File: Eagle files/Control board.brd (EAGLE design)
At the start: 43.2 x 43.2 mm, 27 parts

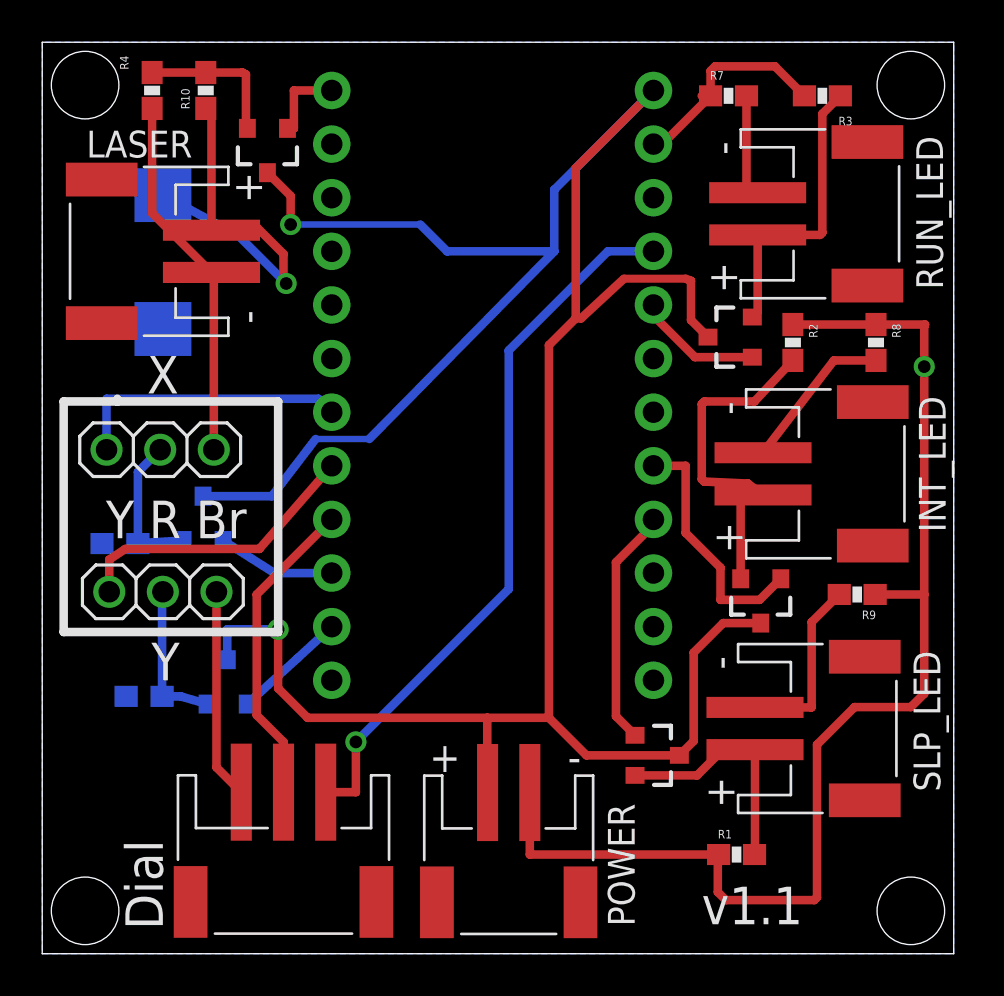
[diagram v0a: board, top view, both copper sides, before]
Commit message: added reverse diode protection on laser
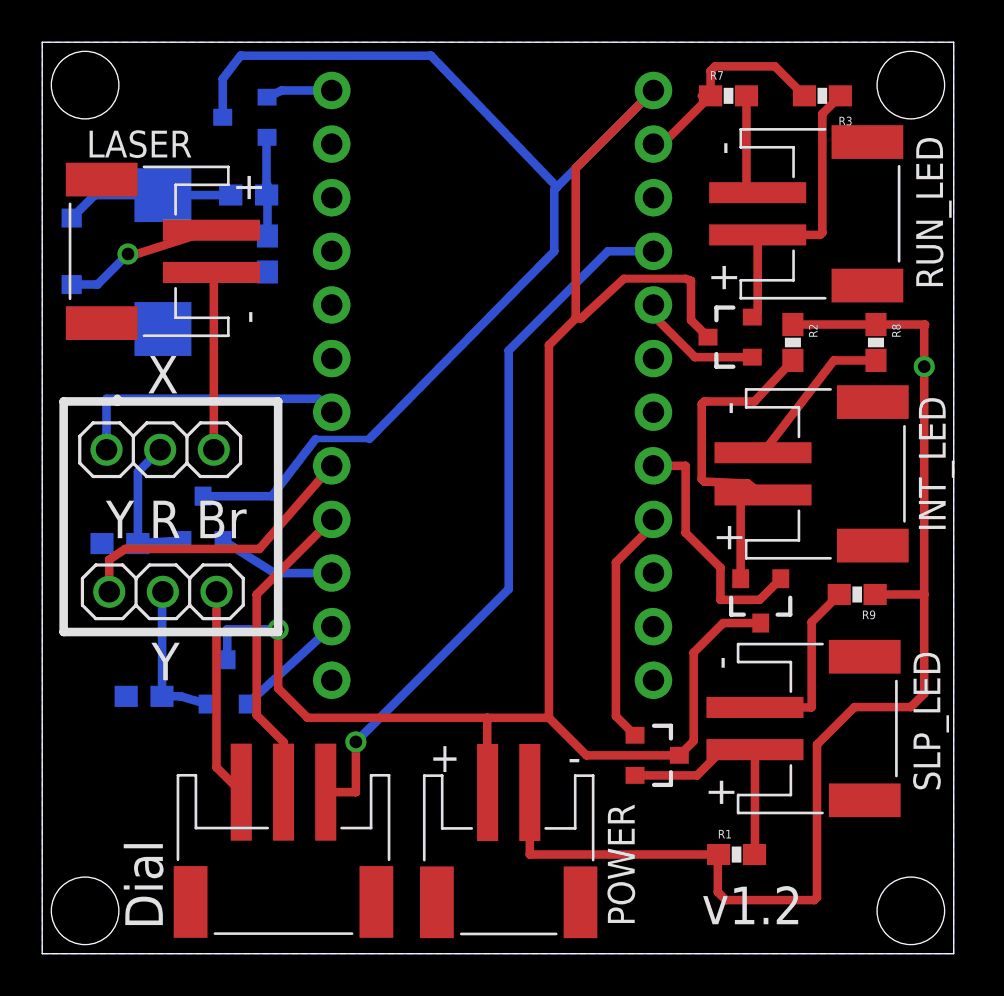
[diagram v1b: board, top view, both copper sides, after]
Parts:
- added D1: (no value), SparkFun-DiscreteSemi:SOD-123
- moved R4 9.48 mm to (10.7, 33.1), flipped to the bottom
- moved R10 5.35 mm to (9.78, 35.9), flipped to the bottom, turned to 180 degrees
- moved LASER_MOS 1.83 mm to (9.65, 39.6), flipped to the bottom, turned to 270 degrees
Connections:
- new net N$2: D1.C, LASER.1
- net N$1: now also D1.A; no longer LASER.1
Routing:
- net N$1: track 18.6 -> 7.98 mm, vias 1 -> 0
- net GND: track 96.0 -> 87.1 mm
- net N$2: track 0.00 -> 7.40 mm, vias 0 -> 1
- net VBAT: track 127.6 -> 132.5 mm, vias 2 -> 1
- net LASER_PWR: track 7.05 -> 5.21 mm
- net LASER_PIN: track 3.89 -> 3.13 mm
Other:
- board text added: "v1.2"
- board text removed: "v1.1"
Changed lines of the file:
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@@
 <wire x1="3.556" y1="26.162" x2="3.556" y2="26.289" width="0.4064" layer="25"/>
 <wire x1="43.18" y1="0" x2="43.18" y2="43.18" width="0" layer="20"/>
-<text x="31.242" y="1.397" size="1.778" layer="25">v1.1</text>
+<text x="31.242" y="1.397" size="1.778" layer="25">v1.2</text>
 </plain>
 <attributes>
@@
 <attribute name="NAME" x="37.719" y="39.243" size="0.4064" layer="25" font="vector"/>
 </element>
-<element name="LASER_MOS" library="SparkFun-DiscreteSemi" package="SOT23-3" value="200mA/50V" x="10.668" y="38.1" smashed="yes" rot="R180">
-<attribute name="PROD_ID" value="TRANS-00830" x="13.843" y="34.163" size="1.778" layer="27" rot="R180" display="off"/>
-</element>
-<element name="R4" library="SparkFun-Resistors" package="0603-RES" value="10K" x="5.207" y="40.894" smashed="yes" rot="R90">
-<attribute name="PROD_ID" value="RES-00824" x="1.27" y="37.719" size="1.778" layer="27" rot="R90" display="off"/>
-<attribute name="NAME" x="3.683" y="42.545" size="0.4064" layer="25" font="vector" rot="R270"/>
+<element name="LASER_MOS" library="SparkFun-DiscreteSemi" package="SOT23-3" value="200mA/50V" x="9.652" y="39.624" smashed="yes" rot="MR270">
+<attribute name="PROD_ID" value="TRANS-00830" x="5.715" y="42.799" size="1.778" layer="28" rot="MR270" display="off"/>
+</element>
+<element name="R4" library="SparkFun-Resistors" package="0603-RES" value="10K" x="10.668" y="33.147" smashed="yes" rot="MR90">
+<attribute name="PROD_ID" value="RES-00824" x="14.605" y="29.972" size="1.778" layer="28" rot="MR90" display="off"/>
+<attribute name="NAME" x="12.192" y="34.798" size="0.4064" layer="26" font="vector" rot="MR270"/>
 </element>
 <element name="X_MOS" library="SparkFun-DiscreteSemi" package="SOT23-3" value="2.6A/20V" x="7.62" y="20.574" smashed="yes" rot="MR0">
@@
 <attribute name="NAME" x="39.497" y="16.256" size="0.4064" layer="25" font="vector" rot="R180"/>
 </element>
-<element name="R10" library="SparkFun-Resistors" package="0603-RES" value="39" x="7.747" y="40.894" rot="R90">
-<attribute name="PROD_ID" value="RES-00824" x="7.747" y="40.894" size="1.778" layer="27" rot="R90" display="off"/>
+<element name="R10" library="SparkFun-Resistors" package="0603-RES" value="39" x="9.779" y="35.941" rot="MR180">
+<attribute name="PROD_ID" value="RES-00824" x="9.779" y="35.941" size="1.778" layer="28" rot="MR180" display="off"/>
 </element>
 <element name="C1" library="SparkFun-Capacitors" package="EIA7343" value="100uF" x="5.715" y="32.766" rot="MR90">
 <attribute name="PROD_ID" value="CAP-07890" x="5.715" y="32.766" size="1.778" layer="28" rot="MR90" display="off"/>
 </element>
+<element name="D1" library="SparkFun-DiscreteSemi" package="SOD-123" value="" x="1.397" y="33.274" rot="MR90"/>
 </elements>
 <signals>
@@
 <wire x1="41.148" y1="11.684" x2="41.783" y2="12.319" width="0.4064" layer="1"/>
 <wire x1="41.783" y1="12.319" x2="41.783" y2="17.018" width="0.4064" layer="1"/>
-<wire x1="8.128" y1="23.876" x2="8.128" y2="32.164" width="0.4064" layer="1"/>
 <wire x1="9.43" y1="7.653" x2="8.255" y2="8.828" width="0.4064" layer="1"/>
 <wire x1="8.255" y1="8.828" x2="8.255" y2="17.145" width="0.4064" layer="1"/>
@@
 <wire x1="8.128" y1="32.164" x2="7.747" y2="32.164" width="0.4064" layer="1"/>
 <wire x1="7.747" y1="32.274" x2="7.747" y2="32.164" width="0.4064" layer="1"/>
-<wire x1="8.018" y1="32.274" x2="5.207" y2="35.085" width="0.4064" layer="1"/>
-<wire x1="5.207" y1="35.085" x2="5.207" y2="40.044" width="0.4064" layer="1"/>
 <contactref element="JP1" pad="2"/>
 <wire x1="28.956" y1="38.354" x2="29.376" y2="38.354" width="0.4064" layer="1"/>
 <wire x1="29.376" y1="38.354" x2="31.662" y2="40.64" width="0.4064" layer="1"/>
+<wire x1="8.128" y1="32.164" x2="8.128" y2="23.876" width="0.4064" layer="1"/>
 <wire x1="8.128" y1="32.164" x2="8.018" y2="32.274" width="0" layer="19" extent="1-1"/>
 </signal>
@@
 <contactref element="JP4" pad="1"/>
 <contactref element="LASER_MOS" pad="1"/>
-<wire x1="11.618" y1="39.1" x2="11.922" y2="39.1" width="0.4064" layer="1"/>
-<wire x1="11.922" y1="39.1" x2="11.922" y2="40.894" width="0.4064" layer="1"/>
-<wire x1="11.922" y1="40.894" x2="13.716" y2="40.894" width="0.4064" layer="1"/>
+<wire x1="10.652" y1="40.574" x2="11.348" y2="40.894" width="0.4064" layer="16"/>
+<wire x1="11.348" y1="40.894" x2="13.716" y2="40.894" width="0.4064" layer="16"/>
 </signal>
 <signal name="AREF">
@@
 <contactref element="R4" pad="2"/>
 <contactref element="R10" pad="2"/>
-<wire x1="9.718" y1="39.1" x2="9.652" y2="39.166" width="0.4064" layer="1"/>
-<wire x1="9.652" y1="39.166" x2="9.652" y2="41.656" width="0.4064" layer="1"/>
-<wire x1="9.652" y1="41.656" x2="9.486" y2="41.744" width="0.4064" layer="1"/>
-<wire x1="9.486" y1="41.744" x2="7.747" y2="41.744" width="0.4064" layer="1"/>
-<wire x1="7.747" y1="41.744" x2="5.207" y2="41.744" width="0.4064" layer="1"/>
+<wire x1="10.629" y1="35.941" x2="10.629" y2="36.449" width="0.4064" layer="16"/>
+<wire x1="10.629" y1="36.449" x2="10.629" y2="38.651" width="0.4064" layer="16"/>
+<wire x1="10.629" y1="38.651" x2="10.652" y2="38.674" width="0.4064" layer="16"/>
+<wire x1="10.668" y1="33.997" x2="10.668" y2="36.41" width="0.4064" layer="16"/>
+<wire x1="10.668" y1="36.41" x2="10.629" y2="36.449" width="0.4064" layer="16"/>
 </signal>
 <signal name="N$7">
@@
 <signal name="N$1">
 <contactref element="R10" pad="1"/>
-<contactref element="LASER" pad="1"/>
 <contactref element="C1" pad="A"/>
-<via x="11.557" y="31.75" extent="1-16" drill="0.6"/>
-<wire x1="7.747" y1="40.044" x2="8.018" y2="39.773" width="0.4064" layer="1"/>
-<wire x1="8.018" y1="39.773" x2="8.018" y2="34.274" width="0.4064" layer="1"/>
-<wire x1="11.557" y1="31.75" x2="11.43" y2="31.877" width="0.4064" layer="1"/>
-<wire x1="11.43" y1="31.877" x2="11.43" y2="33.147" width="0.4064" layer="1"/>
-<wire x1="11.43" y1="33.147" x2="10.16" y2="34.417" width="0.4064" layer="1"/>
-<wire x1="10.16" y1="34.417" x2="8.89" y2="34.417" width="0.4064" layer="1"/>
-<wire x1="8.89" y1="34.417" x2="8.747" y2="34.274" width="0.4064" layer="1"/>
-<wire x1="8.747" y1="34.274" x2="8.018" y2="34.274" width="0.4064" layer="1"/>
-<wire x1="5.715" y1="35.936" x2="9.266" y2="34.041" width="0.4064" layer="16"/>
-<wire x1="9.266" y1="34.041" x2="11.557" y2="31.75" width="0.4064" layer="16"/>
+<contactref element="D1" pad="A"/>
+<wire x1="1.397" y1="34.849" x2="2.484" y2="35.936" width="0.4064" layer="16"/>
+<wire x1="2.484" y1="35.936" x2="5.715" y2="35.936" width="0.4064" layer="16"/>
+<wire x1="8.929" y1="35.941" x2="8.924" y2="35.936" width="0.4064" layer="16"/>
+<wire x1="8.924" y1="35.936" x2="5.715" y2="35.936" width="0.4064" layer="16"/>
 </signal>
 <signal name="5V">
@@
 <wire x1="11.176" y1="15.367" x2="8.763" y2="15.367" width="0.4064" layer="16"/>
 <wire x1="8.763" y1="15.367" x2="8.763" y2="13.927" width="0.4064" layer="16"/>
-<wire x1="11.768" y1="34.544" x2="17.907" y2="34.544" width="0.3048" layer="16"/>
-<wire x1="17.907" y1="34.544" x2="19.177" y2="33.274" width="0.4064" layer="16"/>
-<wire x1="19.177" y1="33.274" x2="24.257" y2="33.274" width="0.4064" layer="16"/>
-<via x="11.768" y="34.544" extent="1-16" drill="0.6" shape="square"/>
 <wire x1="7.62" y1="21.674" x2="10.879" y2="21.674" width="0.4064" layer="16"/>
 <wire x1="10.879" y1="21.674" x2="12.954" y2="24.384" width="0.4064" layer="16"/>
@@
 <wire x1="21.082" y1="8.272" x2="21.082" y2="11.176" width="0.4064" layer="1"/>
 <wire x1="11.176" y1="12.573" x2="12.573" y2="11.176" width="0.4064" layer="1"/>
-<wire x1="11.768" y1="34.544" x2="11.768" y2="35.9" width="0.4064" layer="1"/>
-<wire x1="11.768" y1="35.9" x2="10.668" y2="37" width="0.4064" layer="1"/>
 <wire x1="24.257" y1="33.274" x2="24.257" y2="36.195" width="0.4064" layer="16"/>
 <wire x1="25.273" y1="30.099" x2="25.273" y2="37.211" width="0.4064" layer="1"/>
@@
 <wire x1="30.734" y1="31.877" x2="30.734" y2="30.015" width="0.4064" layer="1"/>
 <wire x1="30.734" y1="30.015" x2="31.539" y2="29.21" width="0.4064" layer="1"/>
-<wire x1="24.257" y1="36.195" x2="28.956" y2="40.894" width="0.4064" layer="16"/>
+<wire x1="24.257" y1="36.195" x2="24.384" y2="36.322" width="0.4064" layer="16"/>
+<wire x1="24.384" y1="36.322" x2="28.956" y2="40.894" width="0.4064" layer="16"/>
 <wire x1="25.273" y1="37.211" x2="28.956" y2="40.894" width="0.4064" layer="1"/>
+<wire x1="8.552" y1="39.624" x2="8.552" y2="41.445" width="0.4064" layer="16"/>
+<wire x1="8.552" y1="41.445" x2="9.398" y2="42.545" width="0.4064" layer="16"/>
+<wire x1="9.398" y1="42.545" x2="18.415" y2="42.545" width="0.4064" layer="16"/>
+<wire x1="18.415" y1="42.545" x2="24.384" y2="36.322" width="0.4064" layer="16"/>
+</signal>
+<signal name="N$2">
+<contactref element="D1" pad="C"/>
+<contactref element="LASER" pad="1"/>
+<via x="4.064" y="33.147" extent="1-16" drill="0.6"/>
+<wire x1="4.064" y1="33.147" x2="4.429" y2="33.131" width="0.4064" layer="1"/>
+<wire x1="4.429" y1="33.131" x2="8.018" y2="34.274" width="0.4064" layer="1"/>
+<wire x1="1.397" y1="31.699" x2="2.616" y2="31.699" width="0.4064" layer="16"/>
+<wire x1="2.616" y1="31.699" x2="4.064" y2="33.147" width="0.4064" layer="16"/>
 </signal>
 </signals>
